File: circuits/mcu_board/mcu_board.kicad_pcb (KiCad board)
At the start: 2 copper layers, 96.3 x 63 mm, 44 parts, among them J1 USB_B_Micro, J2 Conn_01x13_Pin, J3 Conn_01x03_Pin, SW1 SW_Push, SW10 SW_Push, SW11 SW_Push, SW12 SW_Push, SW13 SW_Push, SW2 SW_Push, SW3 SW_Push, SW4 SW_Push, SW5 SW_Push, SW6 SW_Push, SW7 SW_Push, SW8 SW_Push, SW9 SW_Push, U1 AMS1117-3.3, U4 STM32F302CCTx, Y1 8MHz

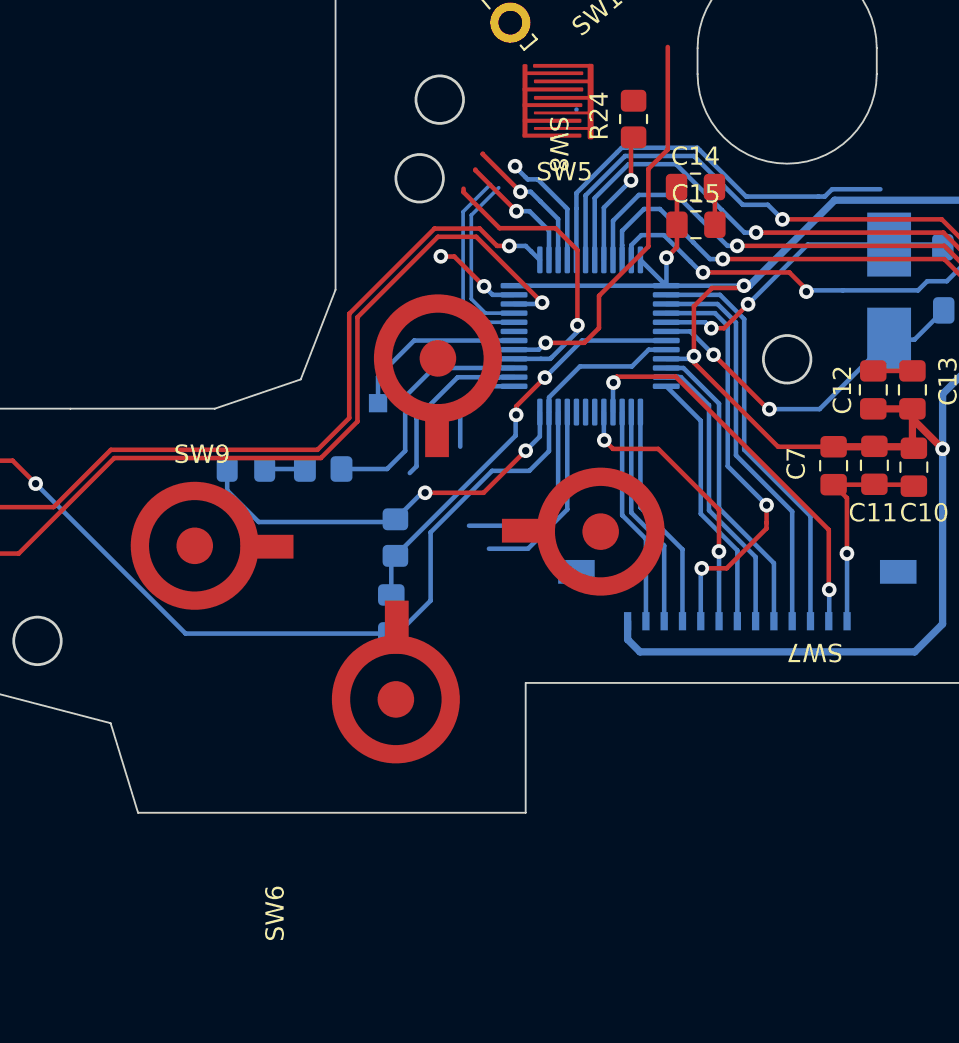
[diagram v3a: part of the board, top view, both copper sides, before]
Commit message: dpad位置对准
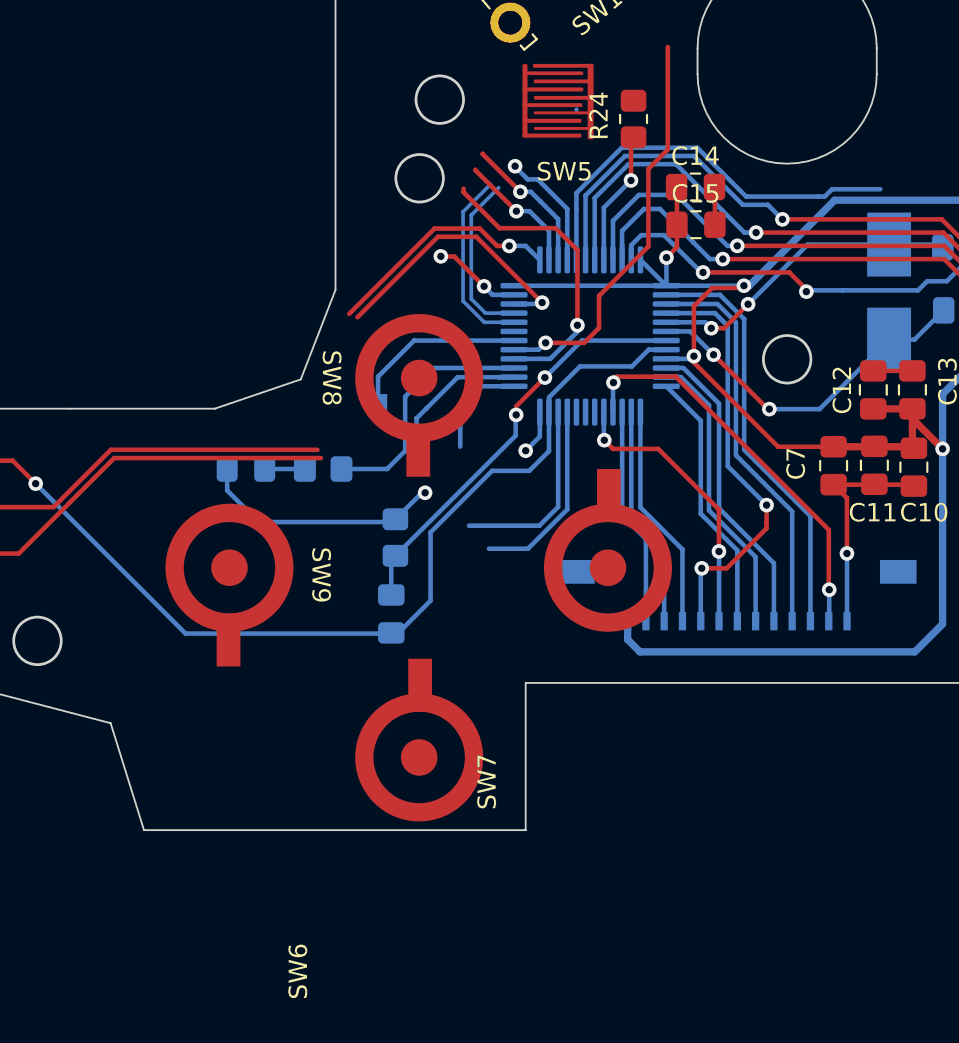
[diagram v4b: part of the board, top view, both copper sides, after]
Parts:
- moved SW6 3.42 mm to (140.9, 136.4)
- moved SW9 2.25 mm to (130.5, 126.0), turned to -90 degrees
- moved SW7 2.02 mm to (151.2, 126.0), turned to 90 degrees
- moved SW8 1.49 mm to (140.9, 115.6)
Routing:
- net /SWDIO: track 44.9 -> 36.3 mm
- net /SWCLK: track 41.5 -> 33.4 mm
- net +3V3: track 170.1 -> 163.7 mm
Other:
- board size 96.3 x 63 mm -> 96.3 x 63.9 mm
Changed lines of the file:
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@@
   )
   (footprint "button:touch-dpad" (layer "F.Cu")
-    (at 150.8 124.025 180)
+    (at 151.2 126 90)
     (property "Sheetfile" "mcu_board.kicad_sch")
     (property "Sheetname" "")
@@
     (property "ki_keywords" "switch normally-open pushbutton push-button")
     (attr smd)
-    (fp_text reference "SW7" (at -11.7 -6.6 180 unlocked) (layer "F.SilkS")
+    (fp_text reference "SW7" (at -11.7 -6.6 90 unlocked) (layer "F.SilkS")
         (effects (font (size 1 1) (thickness 0.1)))
     )
-    (fp_text value "SW_Push" (at -8 6.6 180 unlocked) (layer "F.Fab")
+    (fp_text value "SW_Push" (at -8 6.6 90 unlocked) (layer "F.Fab")
         (effects (font (size 1 1) (thickness 0.15)))
     )
     (fp_rect (start -3.8 -3.8) (end 5.6 3.75)
       (stroke (width 0.1) (type default)) (fill none) (layer "F.Adhes"))
-    (pad "1" smd custom (at 3.95 0.05 180) (size 2.9 1.3) (layers "F.Cu" "F.Paste" "F.Mask")
+    (pad "1" smd custom (at 3.95 0.05 90) (size 2.9 1.3) (layers "F.Cu" "F.Paste" "F.Mask")
       (net 4 "+3V3") (pinfunction "1") (pintype "passive") (thermal_bridge_angle 45)
       (options (clearance outline) (anchor rect))
@@
         (gr_circle (center -3.95 -0.05) (end -0.95 -0.05) (width 1) (fill none))
       ))
-    (pad "2" smd circle (at 0 0 180) (size 2 2) (layers "F.Cu" "F.Paste" "F.Mask")
+    (pad "2" smd circle (at 0 0 90) (size 2 2) (layers "F.Cu" "F.Paste" "F.Mask")
       (net 37 "/BTN_RIGHT") (pinfunction "2") (pintype "passive"))
   )
@@
   )
   (footprint "button:touch-dpad" (layer "F.Cu")
-    (at 139.6 133.2 90)
+    (at 140.875 136.375 90)
     (property "Sheetfile" "mcu_board.kicad_sch")
     (property "Sheetname" "")
@@
   )
   (footprint "button:touch-dpad" (layer "F.Cu")
-    (at 141.9 114.55 -90)
+    (at 140.875 115.625 -90)
     (property "Sheetfile" "mcu_board.kicad_sch")
     (property "Sheetname" "")
@@
     (property "ki_keywords" "switch normally-open pushbutton push-button")
     (attr smd)
-    (fp_text reference "SW8" (at -11.7 -6.6 -90 unlocked) (layer "F.SilkS")
+    (fp_text reference "SW8" (at 0 4.8 -90 unlocked) (layer "F.SilkS")
         (effects (font (size 1 1) (thickness 0.1)))
     )
@@
   )
   (footprint "button:touch-dpad" (layer "F.Cu")
-    (at 128.6 124.8)
+    (at 130.5 126 -90)
     (property "Sheetfile" "mcu_board.kicad_sch")
     (property "Sheetname" "")
@@
     (property "ki_keywords" "switch normally-open pushbutton push-button")
     (attr smd)
-    (fp_text reference "SW9" (at 0.4 -5 unlocked) (layer "F.SilkS")
+    (fp_text reference "SW9" (at 0.4 -5 -90 unlocked) (layer "F.SilkS")
         (effects (font (size 1 1) (thickness 0.1)))
     )
-    (fp_text value "SW_Push" (at -8 6.6 unlocked) (layer "F.Fab")
+    (fp_text value "SW_Push" (at -8 6.6 -90 unlocked) (layer "F.Fab")
         (effects (font (size 1 1) (thickness 0.15)))
     )
     (fp_rect (start -3.8 -3.8) (end 5.6 3.75)
       (stroke (width 0.1) (type default)) (fill none) (layer "F.Adhes"))
-    (pad "1" smd custom (at 3.95 0.05) (size 2.9 1.3) (layers "F.Cu" "F.Paste" "F.Mask")
+    (pad "1" smd custom (at 3.95 0.05 270) (size 2.9 1.3) (layers "F.Cu" "F.Paste" "F.Mask")
       (net 4 "+3V3") (pinfunction "1") (pintype "passive") (thermal_bridge_angle 45)
       (options (clearance outline) (anchor rect))
@@
         (gr_circle (center -3.95 -0.05) (end -0.95 -0.05) (width 1) (fill none))
       ))
-    (pad "2" smd circle (at 0 0) (size 2 2) (layers "F.Cu" "F.Paste" "F.Mask")
+    (pad "2" smd circle (at 0 0 270) (size 2 2) (layers "F.Cu" "F.Paste" "F.Mask")
       (net 36 "/BTN_LEFT") (pinfunction "2") (pintype "passive"))
   )
@@
   (gr_line (start 183.2 80.4) (end 182 79.1)
     (stroke (width 0.1) (type default)) (layer "Edge.Cuts"))
-  (gr_line (start 146.7 132.3) (end 146.7 139.4)
+  (gr_line (start 146.7 132.3) (end 146.7 140.35)
     (stroke (width 0.1) (type default)) (layer "Edge.Cuts"))
   (gr_line (start 175.9 134.8) (end 170.5 129)
@@
   (gr_circle (center 180.9 107.6) (end 182.2 107.6)
     (stroke (width 0.15) (type default)) (fill none) (layer "Edge.Cuts"))
-  (gr_line (start 125.5 139.4) (end 124 134.5)
+  (gr_line (start 125.825 140.35) (end 124 134.5)
     (stroke (width 0.1) (type default)) (layer "Edge.Cuts"))
   (gr_circle (center 161 114.6) (end 162.3 114.6)
@@
   (gr_line (start 196.5 139.4) (end 198.4 134.8)
     (stroke (width 0.1) (type default)) (layer "Edge.Cuts"))
-  (gr_line (start 146.7 139.4) (end 125.5 139.4)
+  (gr_line (start 146.7 140.35) (end 125.825 140.35)
     (stroke (width 0.1) (type default)) (layer "Edge.Cuts"))
   (gr_line (start 166.25 79.1) (end 165.25 76.4)
@@
   (segment (start 167.85 119.3825) (end 163.54 119.3825) (width 0.4) (layer "F.Cu") (net 4))
   (segment (start 154.9725 107.24) (end 154.9725 108.4675) (width 0.25) (layer "F.Cu") (net 4))
-  (segment (start 144.4 121.9) (end 141.2 121.9) (width 0.25) (layer "F.Cu") (net 4))
   (segment (start 154.9725 108.4675) (end 154.4 109.04) (width 0.25) (layer "F.Cu") (net 4))
   (segment (start 167.85 117.85) (end 167.85 117.31) (width 0.4) (layer "F.Cu") (net 4))
@@
   (segment (start 169.5 119.5) (end 167.85 117.85) (width 0.4) (layer "F.Cu") (net 4))
   (segment (start 165.77 117.37) (end 165.71 117.31) (width 0.25) (layer "F.Cu") (net 4))
-  (segment (start 146.7 119.6) (end 144.4 121.9) (width 0.25) (layer "F.Cu") (net 4))
   (segment (start 167.79 117.31) (end 167.85 117.25) (width 0.25) (layer "F.Cu") (net 4))
   (segment (start 155.9 111.7) (end 156.89 110.71) (width 0.25) (layer "F.Cu") (net 4))
@@
   (segment (start 124.2 120) (end 118.975 125.225) (width 0.25) (layer "F.Cu") (net 23))
   (segment (start 118.975 125.225) (end 116.3 125.225) (width 0.25) (layer "F.Cu") (net 23))
-  (segment (start 137.5 118) (end 135.5 120) (width 0.25) (layer "F.Cu") (net 23))
-  (segment (start 137.5 112.3) (end 137.5 118) (width 0.25) (layer "F.Cu") (net 23))
   (segment (start 144 107.9) (end 141.9 107.9) (width 0.25) (layer "F.Cu") (net 23))
   (segment (start 147.6 111.5) (end 144 107.9) (width 0.25) (layer "F.Cu") (net 23))
@@
   (segment (start 124.013604 119.55) (end 120.878604 122.685) (width 0.25) (layer "F.Cu") (net 24))
   (segment (start 141.713604 107.45) (end 137.05 112.113604) (width 0.25) (layer "F.Cu") (net 24))
-  (segment (start 137.05 112.113604) (end 137.05 117.813604) (width 0.25) (layer "F.Cu") (net 24))
-  (segment (start 137.05 117.813604) (end 135.313604 119.55) (width 0.25) (layer "F.Cu") (net 24))
   (segment (start 145.136396 108.4) (end 144.186396 107.45) (width 0.25) (layer "F.Cu") (net 24))
   (segment (start 135.313604 119.55) (end 124.013604 119.55) (width 0.25) (layer "F.Cu") (net 24))

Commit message: 剩下lb rb位置未确定
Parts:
- moved SW3 4.52 mm to (201.2, 111.8)
- moved SW4 3.17 mm to (171.7, 101.6)
- moved SW2 2.16 mm to (201.2, 91.3)
- moved SW1 1.98 mm to (190.3, 101.5)
- moved SW13 1.78 mm to (148.5, 83.1)
- moved SW5 1.74 mm to (149.9, 101.6)
- moved D2 0.20 mm to (160.8, 86.1)
- moved SW10 0.20 mm to (160.8, 86.1)
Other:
- outline, holes or cut-outs redrawn
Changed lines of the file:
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@@
   (net 48 "unconnected-(U4-PA10-Pad31)")
   (footprint "button:touch" (layer "F.Cu")
-    (at 174.52625 100.16)
+    (at 171.7 101.6)
     (property "Sheetfile" "mcu_board.kicad_sch")
     (property "Sheetname" "")
@@
   )
   (footprint "button:touch" (layer "F.Cu")
-    (at 199.1377 91.9323)
+    (at 201.2 91.3)
     (property "Sheetfile" "mcu_board.kicad_sch")
     (property "Sheetname" "")
@@
   )
   (footprint "button:touch" (layer "F.Cu")
-    (at 199.0175 107.84625)
+    (at 201.2 111.805062)
     (property "Sheetfile" "mcu_board.kicad_sch")
     (property "Sheetname" "")
@@
   )
   (footprint "button:click_pair" (layer "F.Cu")
-    (at 150.275 83.235 180)
+    (at 148.5 83.1 180)
     (property "Sheetfile" "mcu_board.kicad_sch")
     (property "Sheetname" "")
@@
   )
   (footprint "button:touch" (layer "F.Cu")
-    (at 148.550125 100.505063)
+    (at 149.9 101.6)
     (property "Sheetfile" "mcu_board.kicad_sch")
     (property "Sheetname" "")
@@
   )
   (footprint "button:touch" (layer "F.Cu")
-    (at 188.660125 100.385062)
+    (at 190.3 101.5)
     (property "Sheetfile" "mcu_board.kicad_sch")
     (property "Sheetname" "")
@@
   )
   (footprint "LED_SMD:LED_0805_2012Metric_Pad1.15x1.40mm_HandSolder" (layer "F.Cu")
-    (at 161 86.1 180)
+    (at 160.8 86.1 180)
     (descr "LED SMD 0805 (2012 Metric), square (rectangular) end terminal, IPC_7351 nominal, (Body size source: https://docs.google.com/spreadsheets/d/1BsfQQcO9C6DZCsRaXUlFlo91Tg2WpOkGARC1WS5S8t0/edit?usp=sharing), generated with kicad-footprint-generator")
     (tags "LED handsolder")
@@
   )
   (footprint "button:touch-xbox" (layer "F.Cu")
-    (at 161 86.1 180)
+    (at 160.8 86.1 180)
     (property "Sheetfile" "mcu_board.kicad_sch")
     (property "Sheetname" "")
@@
   (gr_line (start 186 115.5) (end 174.5 115.5)
     (stroke (width 0.1) (type default)) (layer "Edge.Cuts"))
-  (gr_line (start 165.9 99) (end 165.9 97.58)
+  (gr_line (start 165.7 98.8) (end 165.7 97.38)
     (stroke (width 0.1) (type default)) (layer "Edge.Cuts"))
   (gr_line (start 174.5 115.5) (end 170.5 119.8)
@@
   (gr_line (start 209.2 109.5) (end 209.2 132.6)
     (stroke (width 0.1) (type default)) (layer "Edge.Cuts"))
-  (gr_line (start 156.1 97.58) (end 156.1 99)
-    (stroke (width 0.1) (type default)) (layer "Edge.Cuts"))
-  (gr_arc (start 156.1 97.58) (mid 161 92.68) (end 165.9 97.58)
+  (gr_line (start 155.9 97.38) (end 155.9 98.8)
+    (stroke (width 0.1) (type default)) (layer "Edge.Cuts"))
+  (gr_arc (start 155.9 97.38) (mid 160.8 92.48) (end 165.7 97.38)
     (stroke (width 0.1) (type default)) (layer "Edge.Cuts"))
   (gr_circle (center 201.5 130) (end 202.8 130)
@@
   (gr_line (start 125.825 140.35) (end 124 134.5)
     (stroke (width 0.1) (type default)) (layer "Edge.Cuts"))
-  (gr_circle (center 161 114.6) (end 162.3 114.6)
+  (gr_circle (center 160.8 114.6) (end 162.1 114.6)
     (stroke (width 0.15) (type default)) (fill none) (layer "Edge.Cuts"))
   (gr_line (start 173.3 139.4) (end 173.3 134.1)
@@
   (gr_circle (center 140.9 104.7) (end 142.2 104.7)
     (stroke (width 0.15) (type default)) (fill none) (layer "Edge.Cuts"))
-  (gr_circle (center 199.8 101.5) (end 201.1 101.5)
+  (gr_circle (center 199.9 101.5) (end 201.2 101.5)
     (stroke (width 0.15) (type default)) (fill none) (layer "Edge.Cuts"))
   (gr_line (start 156.2 76.4) (end 165.25 76.4)
@@
   (gr_circle (center 120 130) (end 121.3 130)
     (stroke (width 0.15) (type default)) (fill none) (layer "Edge.Cuts"))
-  (gr_arc (start 165.9 99) (mid 161 103.9) (end 156.1 99)
+  (gr_arc (start 165.7 98.8) (mid 160.8 103.7) (end 155.9 98.8)
     (stroke (width 0.1) (type default)) (layer "Edge.Cuts"))
   (gr_line (start 124 134.5) (end 112.9 131.6)

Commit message: 布局基本确定
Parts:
- moved SW11 2.19 mm to (175.9, 91.2)
- moved SW12 1.66 mm to (145.6, 91.2)
- moved SW13 0.10 mm to (148.5, 83.0)
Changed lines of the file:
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@@
   )
   (footprint "button:click_lbrb" (layer "F.Cu")
-    (at 177.4 89.6 -40)
+    (at 175.9 91.2 -40)
     (property "Sheetfile" "mcu_board.kicad_sch")
     (property "Sheetname" "")
@@
   )
   (footprint "button:click_pair" (layer "F.Cu")
-    (at 148.5 83.1 180)
+    (at 148.5 83 180)
     (property "Sheetfile" "mcu_board.kicad_sch")
     (property "Sheetname" "")
@@
   )
   (footprint "button:click_lbrb" (layer "F.Cu")
-    (at 147 92.1 40)
-    (property "Sheetfile" "mcu_board.kicad_sch")
-    (property "Sheetname" "")
+    (at 145.6 91.2 40)
+    (property "Sheetfile" "mcu_board.kicad_sch")
+    (property "Sheetname" "")

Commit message: layout未完成
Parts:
- R13: moved to F.Cu
- moved R13 18.0 mm to (152.3, 95.3)
- moved R24 6.67 mm to (150.3, 95.2)
- moved R10 2.78 mm to (166.4, 90.1)
- moved R11 1.72 mm to (154.9, 89.1)
- moved R12 1.58 mm to (152.8, 89.1)
- moved C14 0.64 mm to (155.5, 105.6)
- moved C15 0.62 mm to (155.6, 107.7)
- turned D2 to 0 degrees
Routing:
- net GND: track 121.8 -> 200.0 mm, vias 8 -> 10
- net +3V3: track 163.7 -> 221.6 mm, vias 6 -> 8
- net VBUS: track 7.45 -> 62.2 mm, vias 0 -> 2
- net /BTN_XBOX: track 6.64 -> 30.3 mm, vias 1 -> 3
- net /BTN_PAIR: track 16.3 -> 39.8 mm
- net /BTN_RB: track 22.6 -> 42.1 mm
- net /MCU_D+: track 9.36 -> 28.5 mm
- net Net-(J1-Shield): track 0.00 -> 19.1 mm
- net /MCU_D-: track 10.3 -> 29.2 mm
- net /BTN_RM: track 48.2 -> 30.1 mm
- net /BTN_LB: track 7.03 -> 22.0 mm
- net Net-(D2-K): track 0.00 -> 13.2 mm, vias 0 -> 2
- net /D-: track 0.00 -> 10.8 mm
- net /BTN_A: track 43.4 -> 52.4 mm
- net /D+: track 12.5 -> 20.3 mm
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
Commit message: MCU板layout完成
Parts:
- moved D1 43.5 mm to (145.3, 85.4), turned to 180 degrees
- moved U1 39.7 mm to (149.3, 100.1)
- moved C2 38.7 mm to (149.6, 94.5)
- moved C3 36.4 mm to (141.1, 97.0), turned to 180 degrees
- moved R22 8.24 mm to (131.4, 123.7), turned to 180 degrees
- moved C6 6.00 mm to (134.7, 124.8)
- moved R10 5.81 mm to (160.8, 88.5)
- moved R11 0.76 mm to (155.2, 88.4)
- moved R12 0.76 mm to (153.1, 88.4)
- turned SW7 to 180 degrees
- turned SW9 to 0 degrees
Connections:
- U4 pad 21: /BTN_DOWN -> /BTN_RIGHT
- U4 pad 22: /BTN_RIGHT -> /BTN_DOWN
- U4 pad 43: /BTN_Y -> /BTN_X
- U4 pad 45: /BTN_X -> /BTN_Y
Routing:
- net +3V3: track 221.6 -> 345.6 mm, vias 8 -> 16
- net GND: track 200.0 -> 258.1 mm, vias 10 -> 127
- net VBUS: track 62.2 -> 30.8 mm, vias 2 -> 0
- net /BTN_Y: track 47.7 -> 68.4 mm, vias 1 -> 3
- net /BTN_LEFT: track 9.41 -> 27.1 mm, vias 0 -> 3
- net /BTN_DOWN: track 10.5 -> 24.3 mm, vias 0 -> 1
- net /SWCLK: track 33.4 -> 41.5 mm
- net /BTN_X: track 44.5 -> 51.7 mm
- net /MCU_D-: track 29.2 -> 33.9 mm
- net /MCU_D+: track 28.5 -> 33.2 mm
- net Net-(U4-NRST): track 22.8 -> 27.2 mm
- net /D+: track 20.3 -> 16.3 mm
- net /SWDIO: track 36.3 -> 39.4 mm
- net /BTN_RIGHT: track 10.5 -> 9.43 mm, vias 0 -> 1
- net /BTN_UP: track 5.65 -> 6.55 mm, vias 0 -> 1
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- added copper zone on B.Cu, net GND
- added copper zone on F.Cu, net GND
